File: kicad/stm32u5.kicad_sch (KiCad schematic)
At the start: 10 parts, among them SW5 BOOTSEL, U12 STM32U535CET6-modified

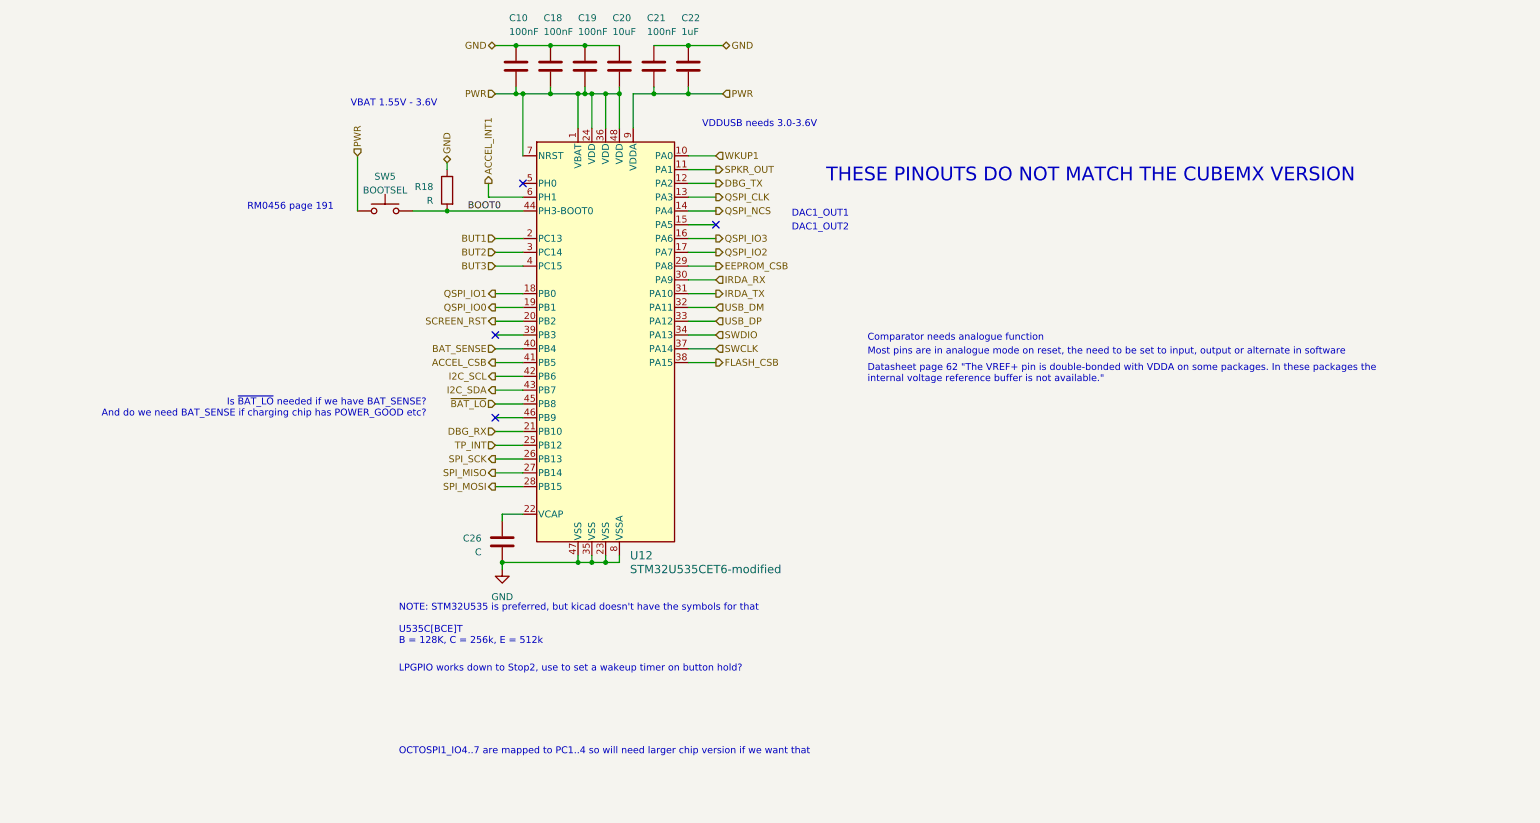
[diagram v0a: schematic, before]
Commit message: Update schematic and add basic PCB layout
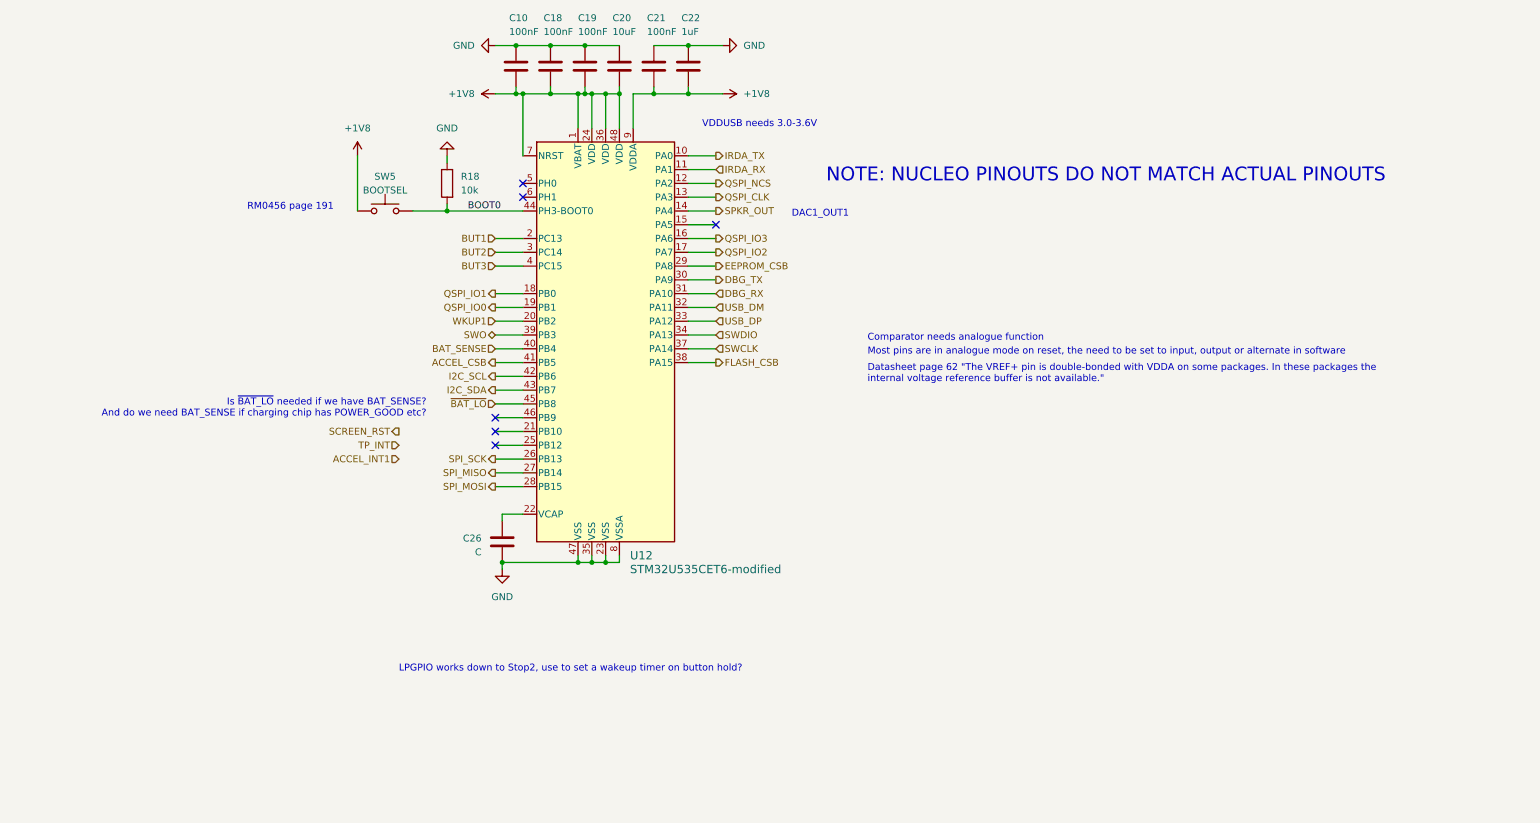
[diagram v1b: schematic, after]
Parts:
- C26: footprint (none) -> Capacitor_SMD:C_0402_1005Metric
- R18: value R -> 10k; footprint (none) -> Capacitor_SMD:C_0402_1005Metric
- U12: footprint LQFP48-7x7mm_STM -> Package_QFP:LQFP-48_7x7mm_P0.5mm
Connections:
- net ACCEL_INT1: no longer U12.6 (PH1)
- net DBG_RX: now also U12.31 (PA10); no longer U12.21 (PB10)
- net DBG_TX: now also U12.30 (PA9); no longer U12.12 (PA2)
- net IRDA_RX: now also U12.11 (PA1); no longer U12.30 (PA9)
- net IRDA_TX: now also U12.10 (PA0); no longer U12.31 (PA10)
- net QSPI_NCS: now also U12.12 (PA2); no longer U12.14 (PA4)
- net SCREEN_RST: no longer U12.20 (PB2)
- net SPKR_OUT: now also U12.14 (PA4); no longer U12.11 (PA1)
- net TP_INT: no longer U12.25 (PB12)
- net WKUP1: now also U12.20 (PB2); no longer U12.10 (PA0)
- net SWO: now reaches U12.39 (PB3)
- net PWR renamed +1V8
- no-connect marks 4 -> 6
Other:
- note added: "NOTE: NUCLEO PINOUTS DO NOT MATCH ACTUAL PINOUTS"
- note removed: "DAC1_OUT2"
- note removed: "NOTE: STM32U535 is preferred, but kicad doesn't have the symbols for that U535C[BCE]T B = 128K, C = 256k, E = 512k"
- note removed: "OCTOSPI1_IO4..7 are mapped to PC1..4 so will need larger chip version if we want that"
- note removed: "THESE PINOUTS DO NOT MATCH THE CUBEMX VERSION"
- note removed: "VBAT 1.55V - 3.6V"
- moved on the sheet: R18

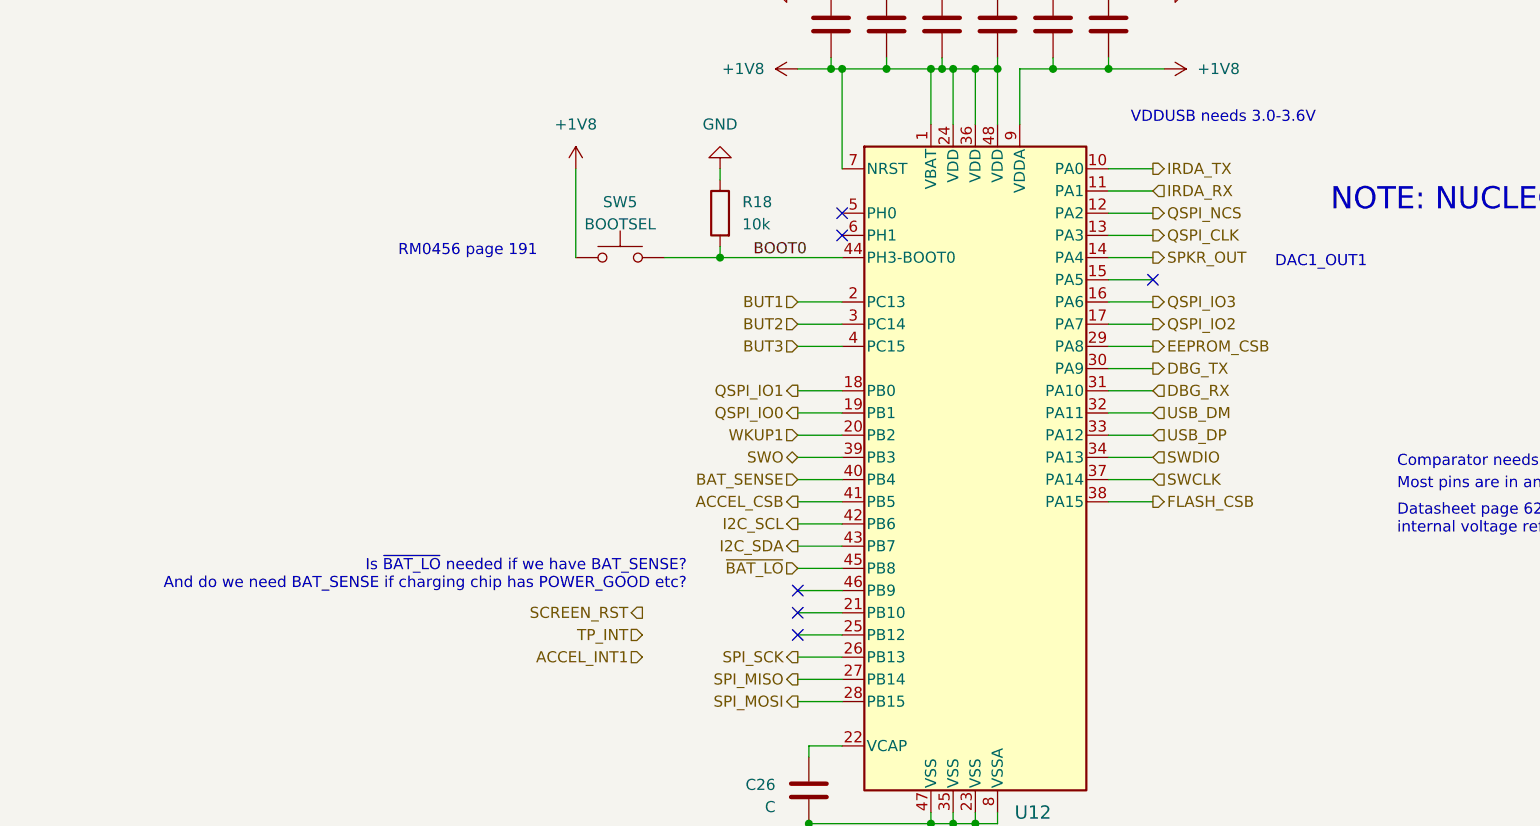
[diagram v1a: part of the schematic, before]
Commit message: Change schematic MCU pinouts
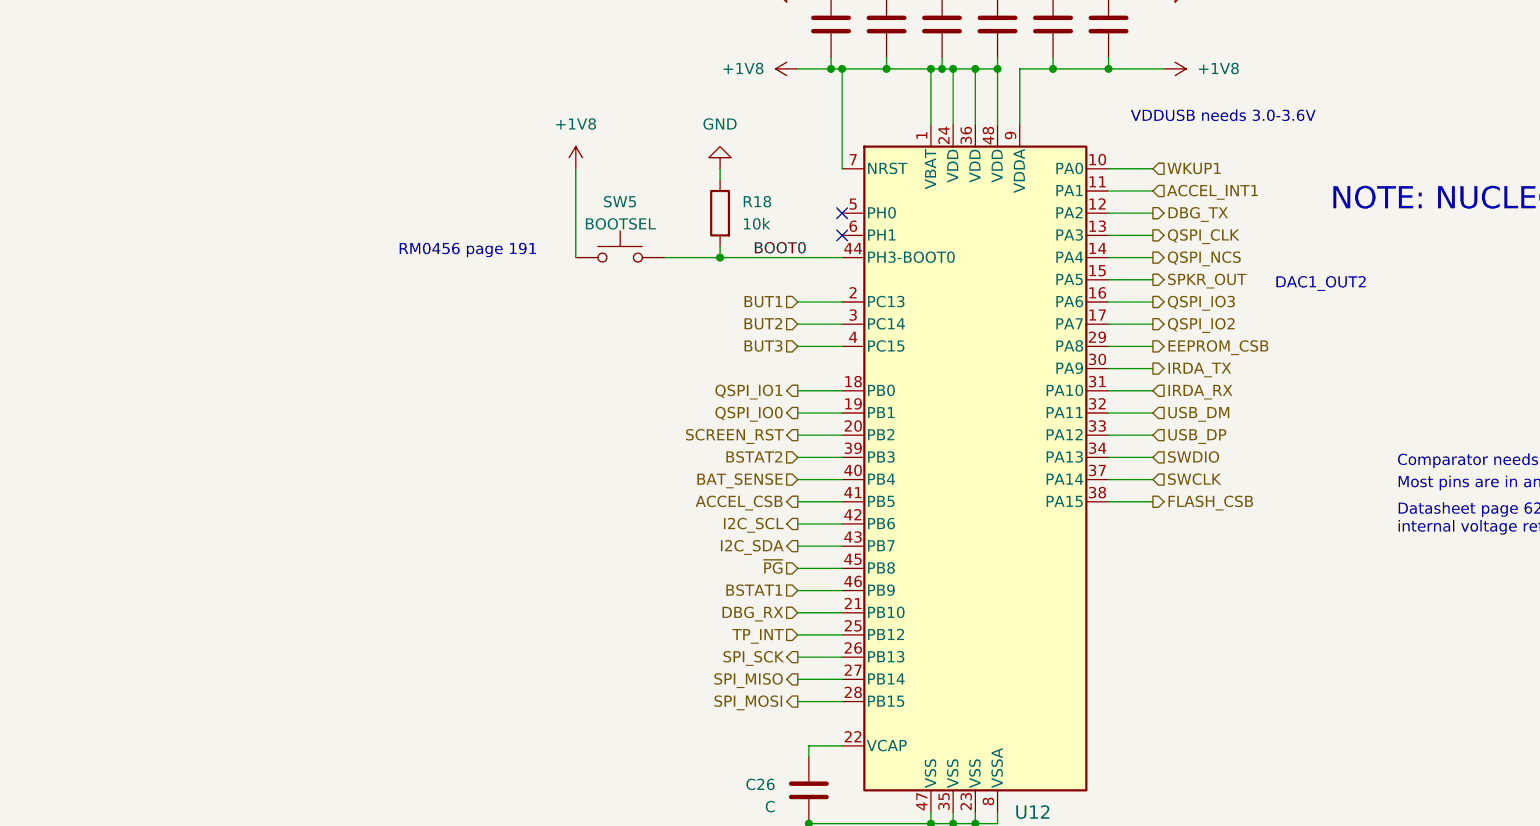
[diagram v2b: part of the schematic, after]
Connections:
- net ACCEL_INT1: now also U12.11 (PA1)
- net DBG_RX: now also U12.21 (PB10); no longer U12.31 (PA10)
- net DBG_TX: now also U12.12 (PA2); no longer U12.30 (PA9)
- net IRDA_RX: now also U12.31 (PA10); no longer U12.11 (PA1)
- net IRDA_TX: now also U12.30 (PA9); no longer U12.10 (PA0)
- net QSPI_NCS: now also U12.14 (PA4); no longer U12.12 (PA2)
- net SCREEN_RST: now also U12.20 (PB2)
- net SPKR_OUT: now also U12.15 (PA5); no longer U12.14 (PA4)
- net TP_INT: now also U12.25 (PB12)
- net WKUP1: now also U12.10 (PA0); no longer U12.20 (PB2)
- net BSTAT1: now reaches U12.46 (PB9)
- net SWO renamed BSTAT2
- net ~{BAT_LO} renamed ~{PG}
- no-connect marks 6 -> 2
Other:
- note added: "DAC1_OUT2"
- note removed: "DAC1_OUT1"
- note removed: "Is ~{BAT_LO} needed if we have BAT_SENSE? And do we need BAT_SENSE if charging chip has POWER_GOOD etc?"
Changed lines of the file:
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@@
   (junction (at 110.49 33.02) (diameter 0) (color 0 0 0 0)
   )
-  (no_connect (at 95.25 97.79))
   (no_connect (at 100.33 52.07))
-  (no_connect (at 95.25 95.25))
   (no_connect (at 100.33 49.53))
-  (no_connect (at 135.89 57.15))
-  (no_connect (at 95.25 92.71))
   (wire (pts (xy 115.57 33.02) (xy 118.11 33.02))
     (stroke (width 0) (type default))
@@
     (effects (font (size 1.27 1.27)) (justify left bottom))
   )
-  (text "DAC1_OUT1" (at 149.86 55.88 0)
-    (effects (font (size 1.27 1.27)) (justify left bottom))
-  )
-  (text "Is ~{BAT_LO} needed if we have BAT_SENSE?\nAnd do we need BAT_SENSE if charging chip has POWER_GOOD etc?\n"
-    (at 82.55 92.71 0)
-    (effects (font (size 1.27 1.27)) (justify right bottom))
+  (text "DAC1_OUT2" (at 149.86 58.42 0)
+    (effects (font (size 1.27 1.27)) (justify left bottom))
   )
   (text "NOTE: NUCLEO PINOUTS DO NOT MATCH ACTUAL PINOUTS" (at 156.21 49.53 0)
@@
     (effects (font (size 1.27 1.27)) (justify left bottom))
   )
-  (hierarchical_label "IRDA_RX" (shape input) (at 135.89 46.99 0) (fields_autoplaced)
-    (effects (font (size 1.27 1.27)) (justify left))
+  (hierarchical_label "BSTAT1" (shape input) (at 95.25 92.71 180) (fields_autoplaced)
+    (effects (font (size 1.27 1.27)) (justify right))
   )
   (hierarchical_label "ACCEL_CSB" (shape output) (at 95.25 82.55 180) (fields_autoplaced)
     (effects (font (size 1.27 1.27)) (justify right))
   )
-  (hierarchical_label "SCREEN_RST" (shape output) (at 77.47 95.25 180) (fields_autoplaced)
+  (hierarchical_label "SCREEN_RST" (shape output) (at 95.25 74.93 180) (fields_autoplaced)
     (effects (font (size 1.27 1.27)) (justify right))
   )
@@
     (effects (font (size 1.27 1.27)) (justify left))
   )
+  (hierarchical_label "IRDA_TX" (shape output) (at 135.89 67.31 0) (fields_autoplaced)
+    (effects (font (size 1.27 1.27)) (justify left))
+  )
+  (hierarchical_label "QSPI_NCS" (shape output) (at 135.89 54.61 0) (fields_autoplaced)
+    (effects (font (size 1.27 1.27)) (justify left))
+  )
   (hierarchical_label "SWCLK" (shape input) (at 135.89 80.01 0) (fields_autoplaced)
     (effects (font (size 1.27 1.27)) (justify left))
   )
-  (hierarchical_label "SPKR_OUT" (shape output) (at 135.89 54.61 0) (fields_autoplaced)
-    (effects (font (size 1.27 1.27)) (justify left))
-  )
-  (hierarchical_label "QSPI_NCS" (shape output) (at 135.89 49.53 0) (fields_autoplaced)
-    (effects (font (size 1.27 1.27)) (justify left))
-  )
-  (hierarchical_label "DBG_TX" (shape output) (at 135.89 67.31 0) (fields_autoplaced)
+  (hierarchical_label "DBG_TX" (shape output) (at 135.89 49.53 0) (fields_autoplaced)
     (effects (font (size 1.27 1.27)) (justify left))
   )
@@
     (effects (font (size 1.27 1.27)) (justify right))
   )
+  (hierarchical_label "SPKR_OUT" (shape output) (at 135.89 57.15 0) (fields_autoplaced)
+    (effects (font (size 1.27 1.27)) (justify left))
+  )
+  (hierarchical_label "ACCEL_INT1" (shape input) (at 135.89 46.99 0) (fields_autoplaced)
+    (effects (font (size 1.27 1.27)) (justify left))
+  )
+  (hierarchical_label "QSPI_IO1" (shape output) (at 95.25 69.85 180) (fields_autoplaced)
+    (effects (font (size 1.27 1.27)) (justify right))
+  )
+  (hierarchical_label "~{PG}" (shape input) (at 95.25 90.17 180) (fields_autoplaced)
+    (effects (font (size 1.27 1.27)) (justify right))
+  )
+  (hierarchical_label "WKUP1" (shape input) (at 135.89 44.45 0) (fields_autoplaced)
+    (effects (font (size 1.27 1.27)) (justify left))
+  )
+  (hierarchical_label "SPI_MOSI" (shape output) (at 95.25 105.41 180) (fields_autoplaced)
+    (effects (font (size 1.27 1.27)) (justify right))
+  )
+  (hierarchical_label "TP_INT" (shape input) (at 95.25 97.79 180) (fields_autoplaced)
+    (effects (font (size 1.27 1.27)) (justify right))
+  )
+  (hierarchical_label "BUT3" (shape input) (at 95.25 64.77 180) (fields_autoplaced)
+    (effects (font (size 1.27 1.27)) (justify right))
+  )
+  (hierarchical_label "FLASH_CSB" (shape output) (at 135.89 82.55 0) (fields_autoplaced)
+    (effects (font (size 1.27 1.27)) (justify left))
+  )
+  (hierarchical_label "BUT1" (shape input) (at 95.25 59.69 180) (fields_autoplaced)
+    (effects (font (size 1.27 1.27)) (justify right))
+  )
+  (hierarchical_label "QSPI_IO3" (shape output) (at 135.89 59.69 0) (fields_autoplaced)
+    (effects (font (size 1.27 1.27)) (justify left))
+  )
+  (hierarchical_label "USB_DM" (shape input) (at 135.89 72.39 0) (fields_autoplaced)
+    (effects (font (size 1.27 1.27)) (justify left))
+  )
+  (hierarchical_label "IRDA_RX" (shape input) (at 135.89 69.85 0) (fields_autoplaced)
+    (effects (font (size 1.27 1.27)) (justify left))
+  )
+  (hierarchical_label "SPI_MISO" (shape output) (at 95.25 102.87 180) (fields_autoplaced)
+    (effects (font (size 1.27 1.27)) (justify right))
+  )
+  (hierarchical_label "USB_DP" (shape input) (at 135.89 74.93 0) (fields_autoplaced)
+    (effects (font (size 1.27 1.27)) (justify left))
+  )
+  (hierarchical_label "I2C_SCL" (shape output) (at 95.25 85.09 180) (fields_autoplaced)
+    (effects (font (size 1.27 1.27)) (justify right))
+  )
+  (hierarchical_label "BSTAT2" (shape input) (at 95.25 77.47 180) (fields_autoplaced)
+    (effects (font (size 1.27 1.27)) (justify right))
+  )
+  (hierarchical_label "DBG_RX" (shape input) (at 95.25 95.25 180) (fields_autoplaced)
+    (effects (font (size 1.27 1.27)) (justify right))
+  )
+  (hierarchical_label "QSPI_IO2" (shape output) (at 135.89 62.23 0) (fields_autoplaced)
+    (effects (font (size 1.27 1.27)) (justify left))
+  )
   (hierarchical_label "BAT_SENSE" (shape input) (at 95.25 80.01 180) (fields_autoplaced)
     (effects (font (size 1.27 1.27)) (justify right))
   )
-  (hierarchical_label "ACCEL_INT1" (shape input) (at 77.47 100.33 180) (fields_autoplaced)
-    (effects (font (size 1.27 1.27)) (justify right))
-  )
-  (hierarchical_label "QSPI_IO1" (shape output) (at 95.25 69.85 180) (fields_autoplaced)
-    (effects (font (size 1.27 1.27)) (justify right))
-  )
-  (hierarchical_label "IRDA_TX" (shape output) (at 135.89 44.45 0) (fields_autoplaced)
-    (effects (font (size 1.27 1.27)) (justify left))
-  )
-  (hierarchical_label "WKUP1" (shape input) (at 95.25 74.93 180) (fields_autoplaced)
-    (effects (font (size 1.27 1.27)) (justify right))
-  )
-  (hierarchical_label "SWO" (shape bidirectional) (at 95.25 77.47 180) (fields_autoplaced)
-    (effects (font (size 1.27 1.27)) (justify right))
-  )
-  (hierarchical_label "~{BAT_LO}" (shape input) (at 95.25 90.17 180) (fields_autoplaced)
-    (effects (font (size 1.27 1.27)) (justify right))
-  )
-  (hierarchical_label "SPI_MOSI" (shape output) (at 95.25 105.41 180) (fields_autoplaced)
-    (effects (font (size 1.27 1.27)) (justify right))
-  )
-  (hierarchical_label "TP_INT" (shape input) (at 77.47 97.79 180) (fields_autoplaced)
-    (effects (font (size 1.27 1.27)) (justify right))
-  )
-  (hierarchical_label "BUT3" (shape input) (at 95.25 64.77 180) (fields_autoplaced)
-    (effects (font (size 1.27 1.27)) (justify right))
-  )
-  (hierarchical_label "FLASH_CSB" (shape output) (at 135.89 82.55 0) (fields_autoplaced)
-    (effects (font (size 1.27 1.27)) (justify left))
-  )
-  (hierarchical_label "BUT1" (shape input) (at 95.25 59.69 180) (fields_autoplaced)
-    (effects (font (size 1.27 1.27)) (justify right))
-  )
-  (hierarchical_label "DBG_RX" (shape input) (at 135.89 69.85 0) (fields_autoplaced)
-    (effects (font (size 1.27 1.27)) (justify left))
-  )
-  (hierarchical_label "QSPI_IO3" (shape output) (at 135.89 59.69 0) (fields_autoplaced)
-    (effects (font (size 1.27 1.27)) (justify left))
-  )
-  (hierarchical_label "USB_DM" (shape input) (at 135.89 72.39 0) (fields_autoplaced)
-    (effects (font (size 1.27 1.27)) (justify left))
-  )
-  (hierarchical_label "SPI_MISO" (shape output) (at 95.25 102.87 180) (fields_autoplaced)
-    (effects (font (size 1.27 1.27)) (justify right))
-  )
-  (hierarchical_label "USB_DP" (shape input) (at 135.89 74.93 0) (fields_autoplaced)
-    (effects (font (size 1.27 1.27)) (justify left))
-  )
-  (hierarchical_label "I2C_SCL" (shape output) (at 95.25 85.09 180) (fields_autoplaced)
-    (effects (font (size 1.27 1.27)) (justify right))
-  )
-  (hierarchical_label "QSPI_IO2" (shape output) (at 135.89 62.23 0) (fields_autoplaced)
-    (effects (font (size 1.27 1.27)) (justify left))
-  )
   (symbol (lib_id "Device:C") (at 124.46 27.94 0) (unit 1)
